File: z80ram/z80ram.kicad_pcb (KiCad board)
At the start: 2 copper layers, 99.8 x 49.9 mm, 19 parts, among them J1 BUS, J2 BUSEXT, Q1 2N7000, U1 Z80CPU, U2 74HCT574, U3 74HCT257, U4 AS6C4008-55PCN, U5 74HCT138, U6 DS1302+, Y1 32.768kHz

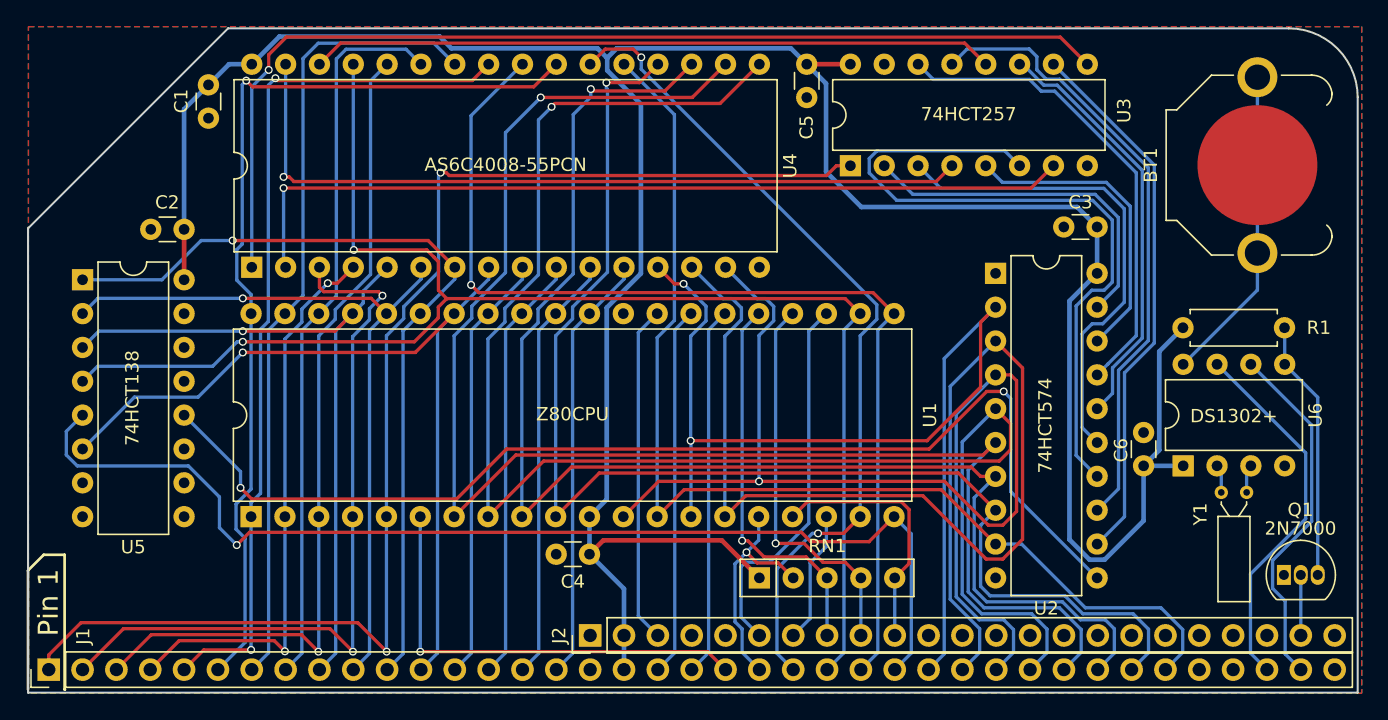
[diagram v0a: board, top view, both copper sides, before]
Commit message: Upgrade Kicad projects to v6
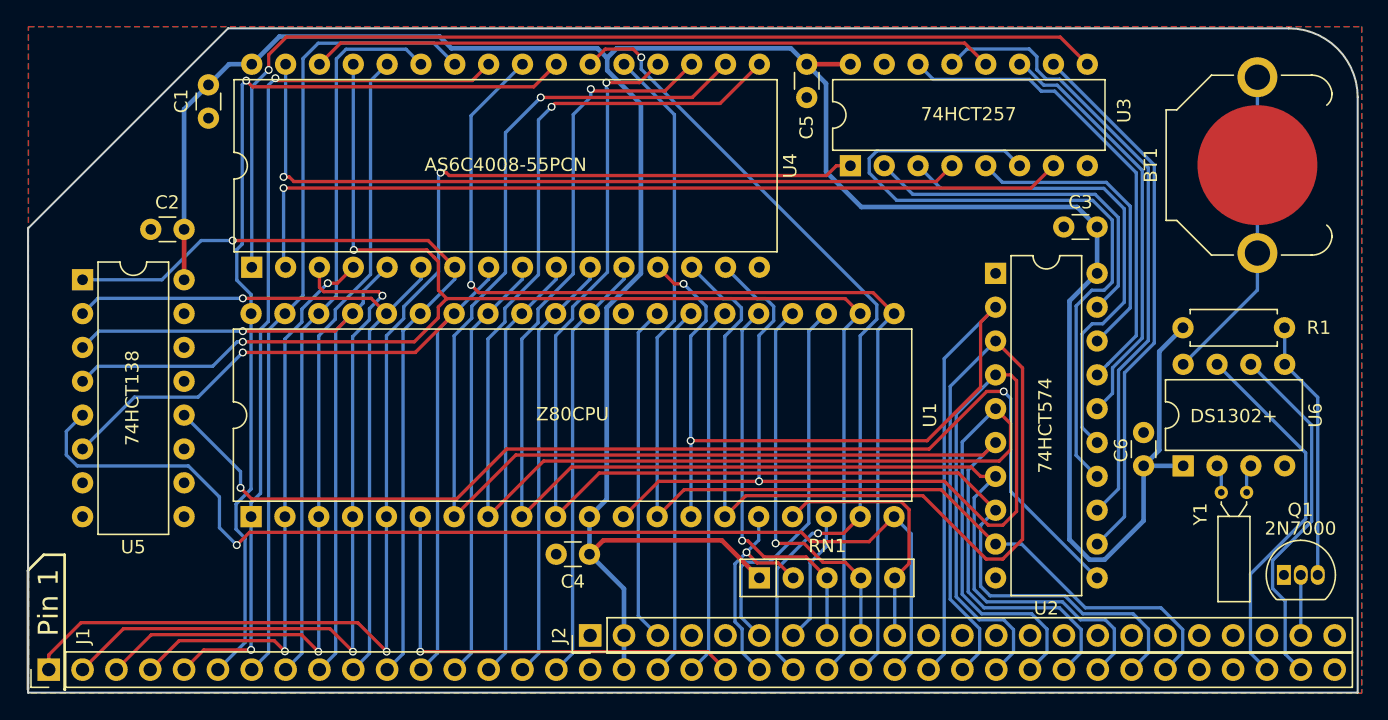
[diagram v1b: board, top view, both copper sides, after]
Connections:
- net /~AUXCS1 renamed /~{AUXCS1}
- net /~BUSACK~ renamed /~{BUSACK}
- net /~BUSRQ renamed /~{BUSRQ}
- net /~HALT renamed /~{HALT}
- net /~INT renamed /~{INT}
- net /~IORQ renamed /~{IORQ}
- net /~M1 renamed /~{M1}
- net /~MREQ renamed /~{MREQ}
- net /~NMI renamed /~{NMI}
- net /~RD renamed /~{RD}
- net /~RFSH renamed /~{RFSH}
- net /~RST renamed /~{RST}
- net /~WAIT renamed /~{WAIT}
- net /~WR renamed /~{WR}
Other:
- net class Default removed
- net class Power removed
